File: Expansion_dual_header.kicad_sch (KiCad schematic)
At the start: 6 parts, among them J3 ESQ-120-14-G-S, J4 ESQ-120-14-G-S, J5 Conn_01x02_Pin, J6 Conn_01x02_Pin

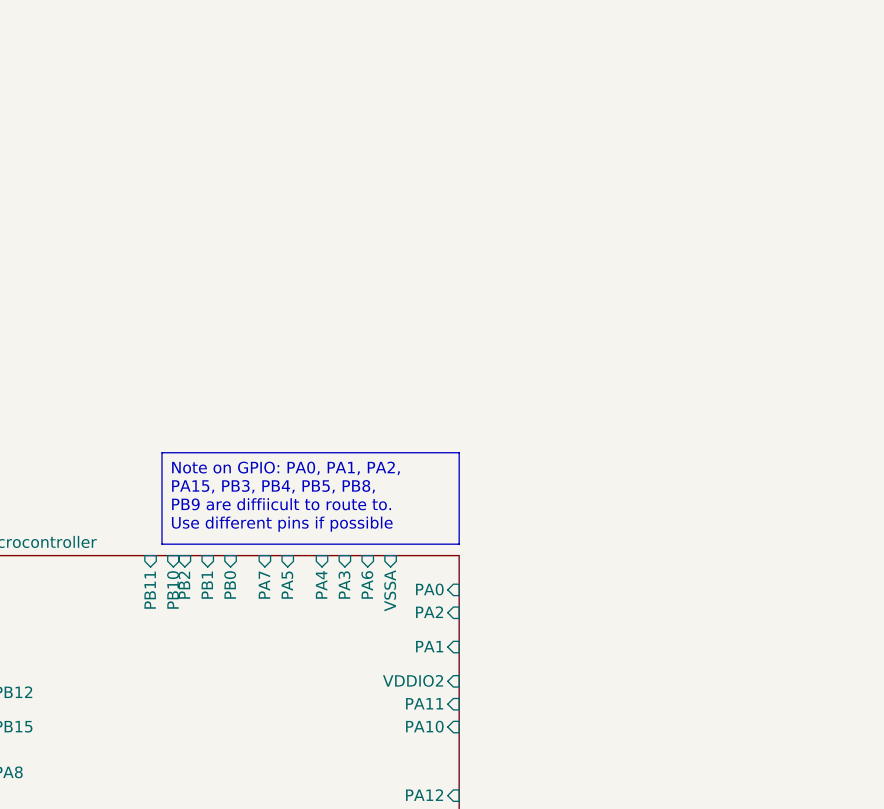
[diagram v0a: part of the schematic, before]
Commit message: Adding components to schematics
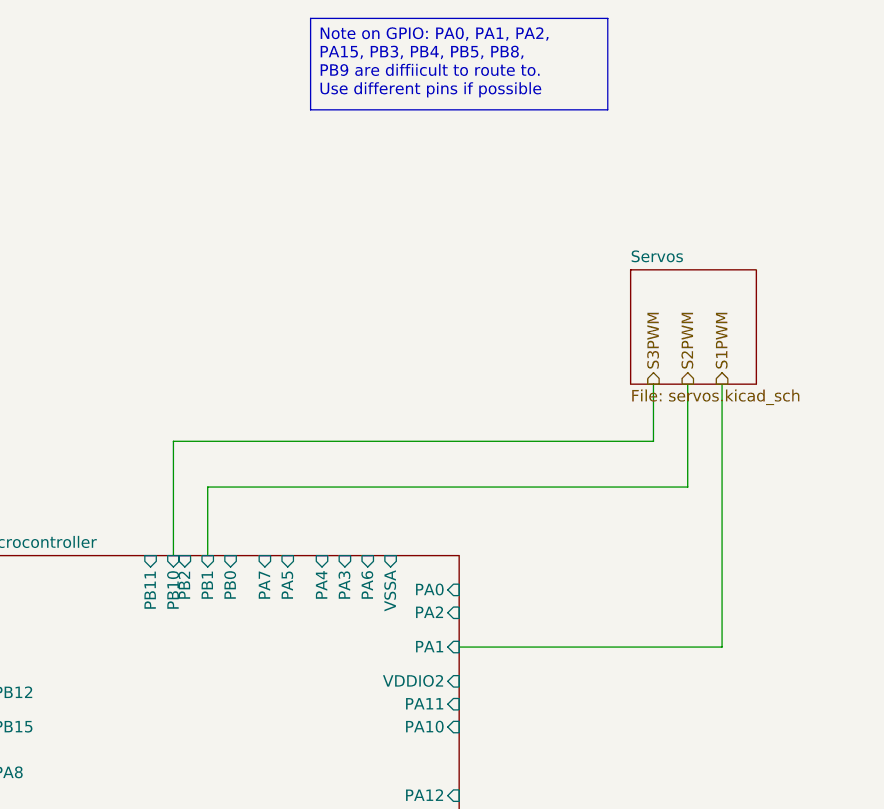
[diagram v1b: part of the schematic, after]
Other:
- added sheet Servos (servos.kicad_sch)
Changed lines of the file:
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@@
 	(text_box "Note on GPIO: PA0, PA1, PA2, PA15, PB3, PB4, PB5, PB8, PB9 are diffiicult to route to. Use different pins if possible"
 		(exclude_from_sim no)
-		(at 212.09 64.77 0)
+		(at 228.6 16.51 0)
 		(size 33.02 10.16)
 		(margins 0.9525 0.9525 0.9525 0.9525)
@@
 	(wire
 		(pts
+			(xy 270.51 57.15) (xy 270.51 68.58)
+		)
+		(stroke
+			(width 0)
+			(type default)
+		)
+	)
+	(wire
+		(pts
 			(xy 54.61 30.48) (xy 54.61 35.56)
 		)
@@
 	(wire
 		(pts
+			(xy 245.11 86.36) (xy 274.32 86.36)
+		)
+		(stroke
+			(width 0)
+			(type default)
+		)
+	)
+	(wire
+		(pts
 			(xy 104.14 74.93) (xy 104.14 85.09)
 		)
@@
 	(wire
 		(pts
+			(xy 266.7 63.5) (xy 213.36 63.5)
+		)
+		(stroke
+			(width 0)
+			(type default)
+		)
+	)
+	(wire
+		(pts
 			(xy 38.1 100.33) (xy 60.96 100.33)
 		)
@@
 	(wire
 		(pts
+			(xy 270.51 68.58) (xy 217.17 68.58)
+		)
+		(stroke
+			(width 0)
+			(type default)
+		)
+	)
+	(wire
+		(pts
 			(xy 78.74 74.93) (xy 78.74 92.71)
 		)
@@
 	(wire
 		(pts
+			(xy 274.32 57.15) (xy 274.32 86.36)
+		)
+		(stroke
+			(width 0)
+			(type default)
+		)
+	)
+	(wire
+		(pts
+			(xy 213.36 63.5) (xy 213.36 76.2)
+		)
+		(stroke
+			(width 0)
+			(type default)
+		)
+	)
+	(wire
+		(pts
 			(xy 81.28 92.71) (xy 81.28 114.3)
 		)
@@
 	(wire
 		(pts
+			(xy 266.7 57.15) (xy 266.7 63.5)
+		)
+		(stroke
+			(width 0)
+			(type default)
+		)
+	)
+	(wire
+		(pts
 			(xy 54.61 38.1) (xy 62.23 38.1)
 		)
@@
 		(pts
 			(xy 55.88 74.93) (xy 55.88 85.09)
+		)
+		(stroke
+			(width 0)
+			(type default)
+		)
+	)
+	(wire
+		(pts
+			(xy 217.17 68.58) (xy 217.17 76.2)
 		)
 		(stroke
@@
 		)
 	)
+	(hierarchical_label "S1PWM"
+		(shape output)
+		(at 274.32 57.15 90)
+		(effects
+			(font
+				(size 1.27 1.27)
+			)
+			(justify left)
+		)
+	)
 	(hierarchical_label "SDA"
 		(shape input)
@@
 			)
 			(justify right)
+		)
+	)
+	(hierarchical_label "S2PWM"
+		(shape output)
+		(at 270.51 57.15 90)
+		(effects
+			(font
+				(size 1.27 1.27)
+			)
+			(justify left)
+		)
+	)
+	(hierarchical_label "S3PWM"
+		(shape output)
+		(at 266.7 57.15 90)
+		(effects
+			(font
+				(size 1.27 1.27)
+			)
+			(justify left)
 		)
 	)
@@
 				)
 			)
+		)
+	)
+	(sheet
+		(at 264.16 44.45)
+		(size 13.97 12.7)
+		(exclude_from_sim no)
+		(in_bom yes)
+		(on_board yes)
+		(dnp no)
+		(fields_autoplaced yes)
+		(stroke
+			(width 0.1524)
+			(type solid)
+		)
+		(fill
+			(color 0 0 0 0.0000)
+		)
+		(property "Sheetname" "Servos"
+			(at 264.16 43.7384 0)
+			(effects
+				(font
+					(size 1.27 1.27)
+				)
+				(justify left bottom)
+			)
+		)
+		(property "Sheetfile" "servos.kicad_sch"
+			(at 264.16 57.7346 0)
+			(effects
+				(font
+					(size 1.27 1.27)
+				)
+				(justify left top)
+			)
+		)
+		(instances
+			(project "Expansion_dual_header"
+				(path "/45910b0a-2ab6-4912-b705-1582171f57d5"
+					(page "4")
+				)
+			)

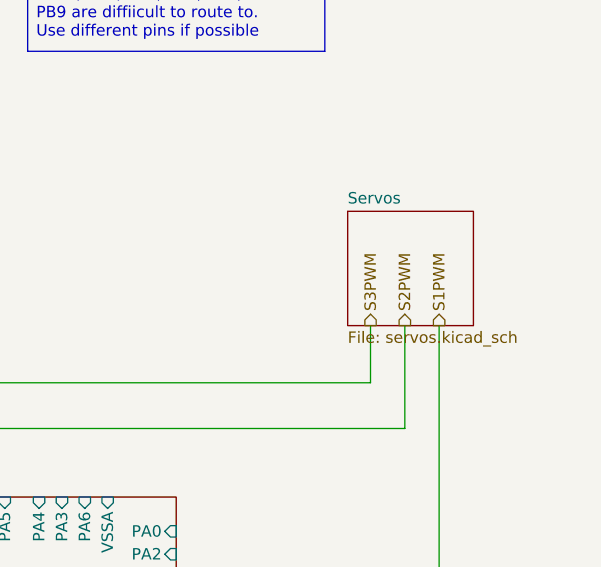
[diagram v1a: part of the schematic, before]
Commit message: Fixed Hierarchy mess
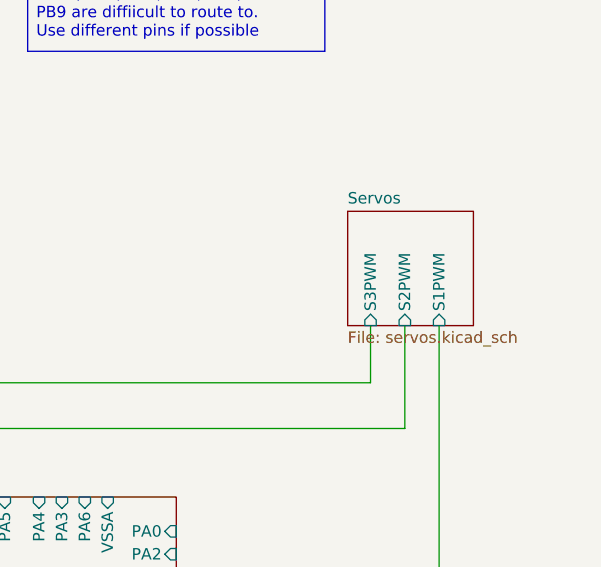
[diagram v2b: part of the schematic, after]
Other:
- sheet Servos ports: added S1PWM, S2PWM, S3PWM; removed none
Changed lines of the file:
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@@
-		)
-	)
-	(hierarchical_label "S1PWM"
-		(shape output)
-		(at 274.32 57.15 90)
-		(effects
-			(font
-				(size 1.27 1.27)
-			)
-			(justify left)
 		)
 	)
@@
 		)
 	)
-	(hierarchical_label "S2PWM"
-		(shape output)
-		(at 270.51 57.15 90)
-		(effects
-			(font
-				(size 1.27 1.27)
-			)
-			(justify left)
-		)
-	)
-	(hierarchical_label "S3PWM"
-		(shape output)
-		(at 266.7 57.15 90)
-		(effects
-			(font
-				(size 1.27 1.27)
-			)
-			(justify left)
-		)
-	)
 	(symbol
 		(lib_id "power:+3V3")
@@
 			)
 		)
+		(pin "S1PWM" input
+			(at 274.32 57.15 270)
+			(effects
+				(font
+					(size 1.27 1.27)
+				)
+				(justify left)
+			)
+		)
+		(pin "S2PWM" input
+			(at 270.51 57.15 270)
+			(effects
+				(font
+					(size 1.27 1.27)
+				)
+				(justify left)
+			)
+		)
+		(pin "S3PWM" input
+			(at 266.7 57.15 270)
+			(effects
+				(font
+					(size 1.27 1.27)
+				)
+				(justify left)
+			)
+		)

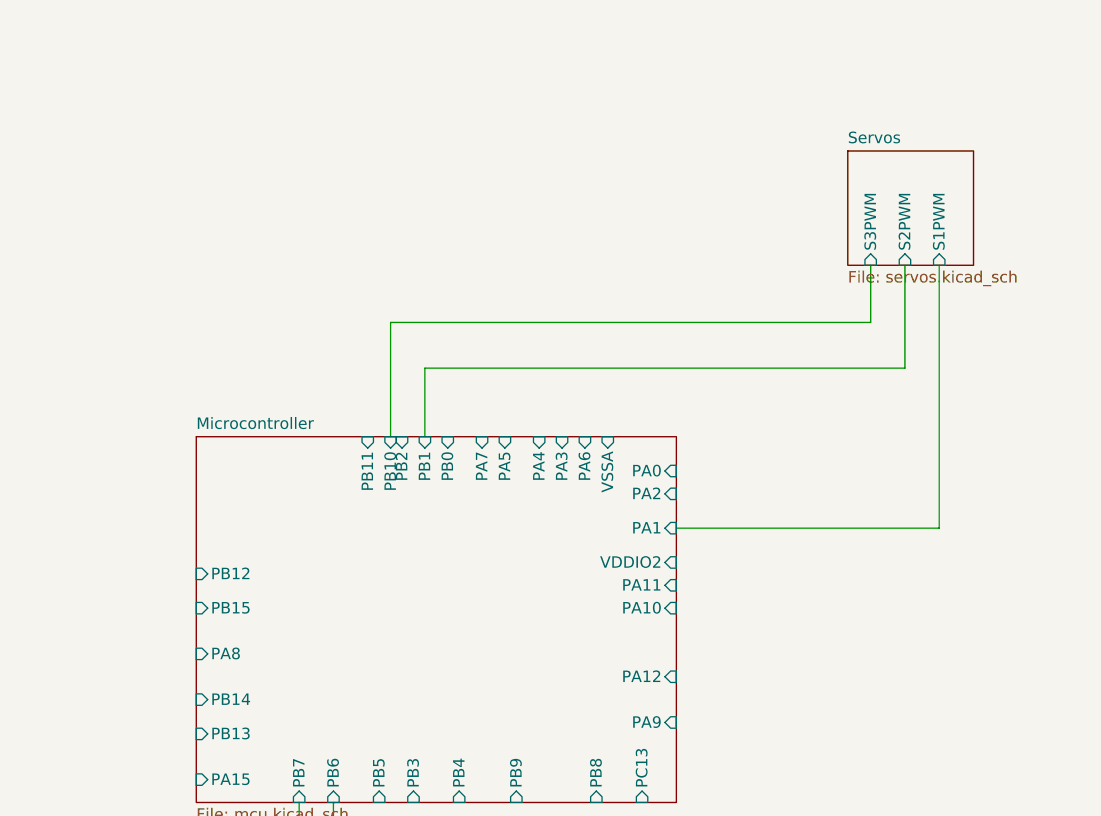
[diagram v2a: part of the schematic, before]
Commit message: added MOSFET, and switch for Servos
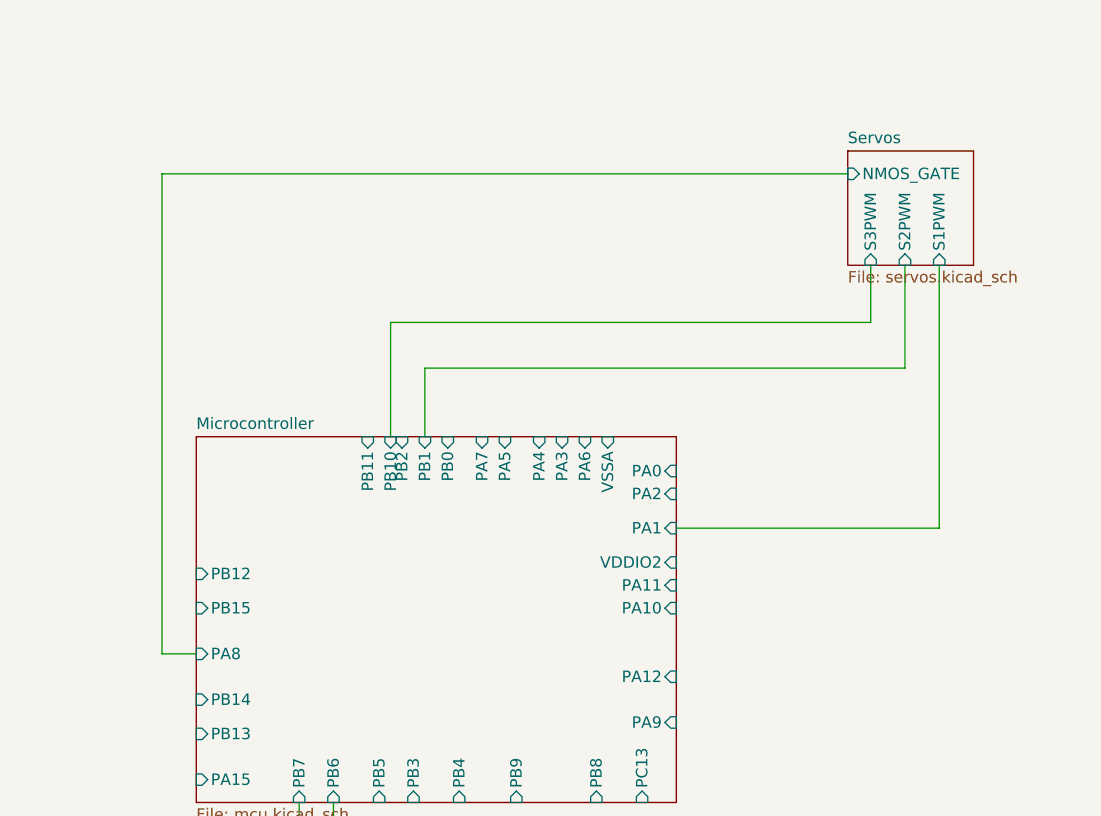
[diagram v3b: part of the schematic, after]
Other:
- sheet Servos ports: added NMOS_GATE; removed none
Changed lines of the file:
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@@
+	(wire
+		(pts
+			(xy 264.16 46.99) (xy 187.96 46.99)
+		)
+		(stroke
+			(width 0)
+			(type default)
+		)
+	)
+	(wire
+		(pts
+			(xy 187.96 100.33) (xy 191.77 100.33)
+		)
+		(stroke
+			(width 0)
+			(type default)
+		)
+	)
 	(wire
 		(pts
@@
 		(pts
 			(xy 68.58 92.71) (xy 68.58 114.3)
+		)
+		(stroke
+			(width 0)
+			(type default)
+		)
+	)
+	(wire
+		(pts
+			(xy 187.96 46.99) (xy 187.96 100.33)
 		)
 		(stroke
@@
 			(effects
 				(font
+					(size 1.27 1.27)
+				)
+				(justify left)
+			)
+		)
+		(pin "NMOS_GATE" input
+			(at 264.16 46.99 180)
+			(effects
+				(font

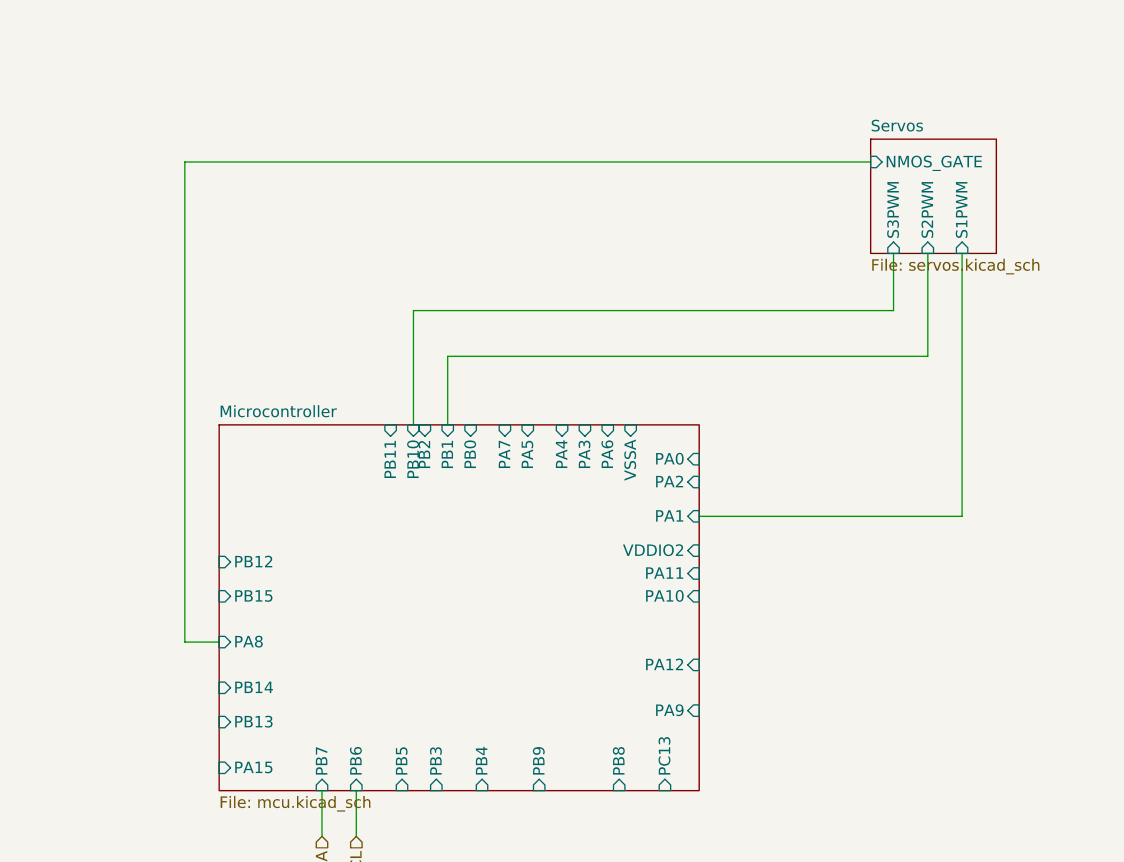
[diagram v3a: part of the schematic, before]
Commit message: add trace lines to PCB
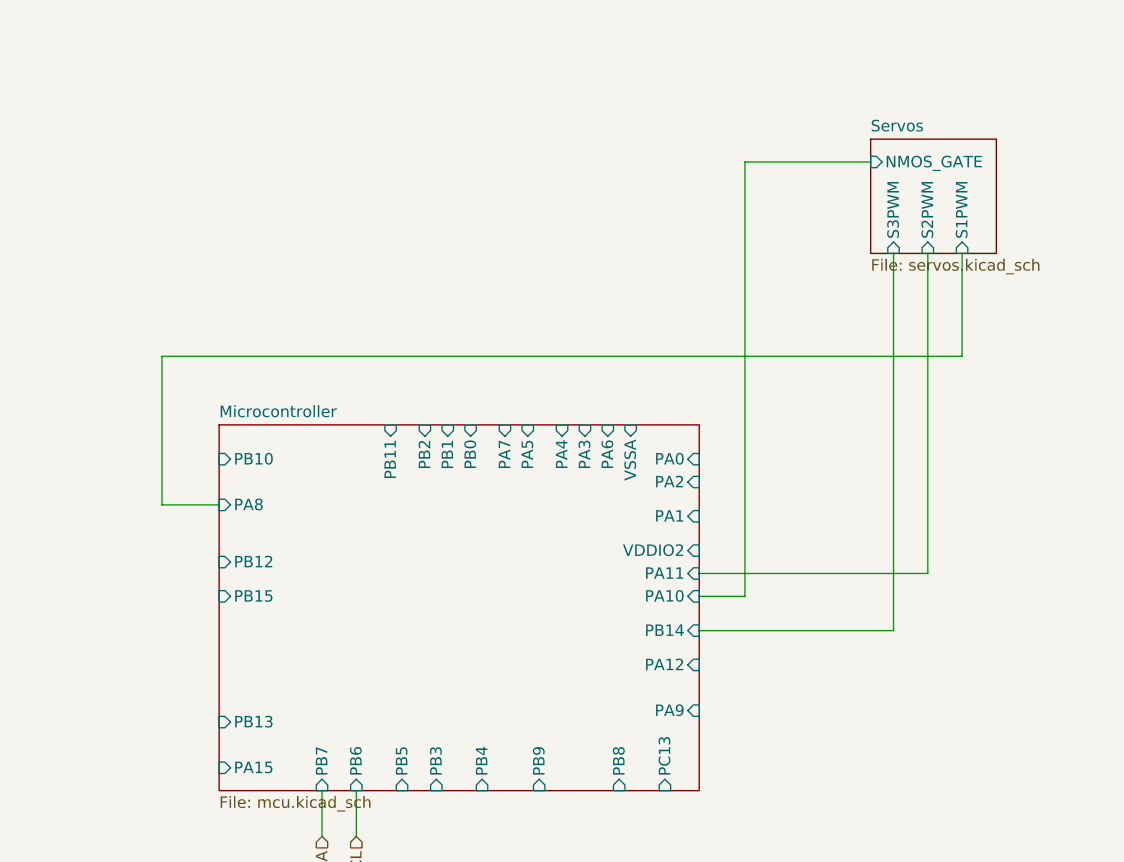
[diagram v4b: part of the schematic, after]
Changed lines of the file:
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@@
-	(wire
-		(pts
-			(xy 270.51 57.15) (xy 270.51 68.58)
-		)
-		(stroke
-			(width 0)
-			(type default)
-		)
-	)
 	(wire
 		(pts
@@
 	(wire
 		(pts
+			(xy 270.51 57.15) (xy 270.51 92.71)
+		)
+		(stroke
+			(width 0)
+			(type default)
+		)
+	)
+	(wire
+		(pts
 			(xy 66.04 74.93) (xy 66.04 100.33)
 		)
@@
 	(wire
 		(pts
-			(xy 245.11 86.36) (xy 274.32 86.36)
-		)
-		(stroke
-			(width 0)
-			(type default)
-		)
-	)
-	(wire
-		(pts
-			(xy 264.16 46.99) (xy 187.96 46.99)
-		)
-		(stroke
-			(width 0)
-			(type default)
-		)
-	)
-	(wire
-		(pts
-			(xy 187.96 100.33) (xy 191.77 100.33)
+			(xy 185.42 85.09) (xy 191.77 85.09)
+		)
+		(stroke
+			(width 0)
+			(type default)
+		)
+	)
+	(wire
+		(pts
+			(xy 185.42 68.58) (xy 185.42 85.09)
 		)
 		(stroke
@@
 	(wire
 		(pts
+			(xy 264.16 46.99) (xy 250.19 46.99)
+		)
+		(stroke
+			(width 0)
+			(type default)
+		)
+	)
+	(wire
+		(pts
 			(xy 58.42 92.71) (xy 68.58 92.71)
 		)
@@
 	(wire
 		(pts
-			(xy 266.7 63.5) (xy 213.36 63.5)
-		)
-		(stroke
-			(width 0)
-			(type default)
-		)
-	)
-	(wire
-		(pts
 			(xy 38.1 100.33) (xy 60.96 100.33)
 		)
@@
 	(wire
 		(pts
-			(xy 270.51 68.58) (xy 217.17 68.58)
-		)
-		(stroke
-			(width 0)
-			(type default)
-		)
-	)
-	(wire
-		(pts
 			(xy 78.74 74.93) (xy 78.74 92.71)
 		)
@@
 	(wire
 		(pts
-			(xy 274.32 57.15) (xy 274.32 86.36)
-		)
-		(stroke
-			(width 0)
-			(type default)
-		)
-	)
-	(wire
-		(pts
-			(xy 213.36 63.5) (xy 213.36 76.2)
-		)
-		(stroke
-			(width 0)
-			(type default)
-		)
-	)
-	(wire
-		(pts
 			(xy 81.28 92.71) (xy 81.28 114.3)
 		)
@@
 	(wire
 		(pts
+			(xy 245.11 92.71) (xy 270.51 92.71)
+		)
+		(stroke
+			(width 0)
+			(type default)
+		)
+	)
+	(wire
+		(pts
 			(xy 101.6 74.93) (xy 101.6 92.71)
 		)
@@
 	(wire
 		(pts
+			(xy 245.11 99.06) (xy 266.7 99.06)
+		)
+		(stroke
+			(width 0)
+			(type default)
+		)
+	)
+	(wire
+		(pts
 			(xy 88.9 107.95) (xy 96.52 107.95)
 		)
@@
 	(wire
 		(pts
+			(xy 250.19 95.25) (xy 245.11 95.25)
+		)
+		(stroke
+			(width 0)
+			(type default)
+		)
+	)
+	(wire
+		(pts
 			(xy 68.58 92.71) (xy 68.58 114.3)
 		)
@@
 	(wire
 		(pts
-			(xy 187.96 46.99) (xy 187.96 100.33)
-		)
-		(stroke
-			(width 0)
-			(type default)
-		)
-	)
-	(wire
-		(pts
 			(xy 71.12 107.95) (xy 71.12 114.3)
 		)
@@
 	(wire
 		(pts
-			(xy 266.7 57.15) (xy 266.7 63.5)
+			(xy 266.7 57.15) (xy 266.7 99.06)
 		)
 		(stroke
@@
 	(wire
 		(pts
-			(xy 217.17 68.58) (xy 217.17 76.2)
-		)
-		(stroke
-			(width 0)
-			(type default)
-		)
-	)
-	(wire
-		(pts
 			(xy 99.06 100.33) (xy 99.06 114.3)
 		)
@@
 	(wire
 		(pts
+			(xy 274.32 57.15) (xy 274.32 68.58)
+		)
+		(stroke
+			(width 0)
+			(type default)
+		)
+	)
+	(wire
+		(pts
+			(xy 250.19 46.99) (xy 250.19 95.25)
+		)
+		(stroke
+			(width 0)
+			(type default)
+		)
+	)
+	(wire
+		(pts
 			(xy 63.5 74.93) (xy 63.5 107.95)
 		)
@@
 		(pts
 			(xy 38.1 92.71) (xy 58.42 92.71)
+		)
+		(stroke
+			(width 0)
+			(type default)
+		)
+	)
+	(wire
+		(pts
+			(xy 274.32 68.58) (xy 185.42 68.58)
 		)
 		(stroke
@@
 		)
 		(pin "PA8" input
-			(at 191.77 100.33 180)
+			(at 191.77 85.09 180)
 			(effects
 				(font
@@
 		)
 		(pin "PB14" input
-			(at 191.77 105.41 180)
-			(effects
-				(font
-					(size 1.27 1.27)
-				)
-				(justify left)
+			(at 245.11 99.06 0)
+			(effects
+				(font
+					(size 1.27 1.27)
+				)
+				(justify right)
 			)
 		)
@@
 		)
 		(pin "PB10" input
-			(at 213.36 76.2 90)
-			(effects
-				(font
-					(size 1.27 1.27)
-				)
-				(justify right)
-			)
-		)
+			(at 191.77 80.01 180)
+			(effects
+				(font
+					(size 1.27 1.27)
+				)
+				(justify left)
+			)
+		)
